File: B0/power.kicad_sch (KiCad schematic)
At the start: 54 parts, among them U001 74HCT00, U002 74HCT125, U007 74HCT32, U008 74HCT04, U009 74HCT00, U010 74HCT125, U011 74HCT04, U012 74HCT00, U013 74HCT125, U014 74HCT08, U015 74HCT04, U016 74HCT00, U017 74HCT125, U018 74HCT04, U019 74HCT00, U020 74HCT125, U021 74HCT08, U028 74HCT00, U029 74HCT00, U030 74HCT32, U031 74HCT00, U032 74HCT74

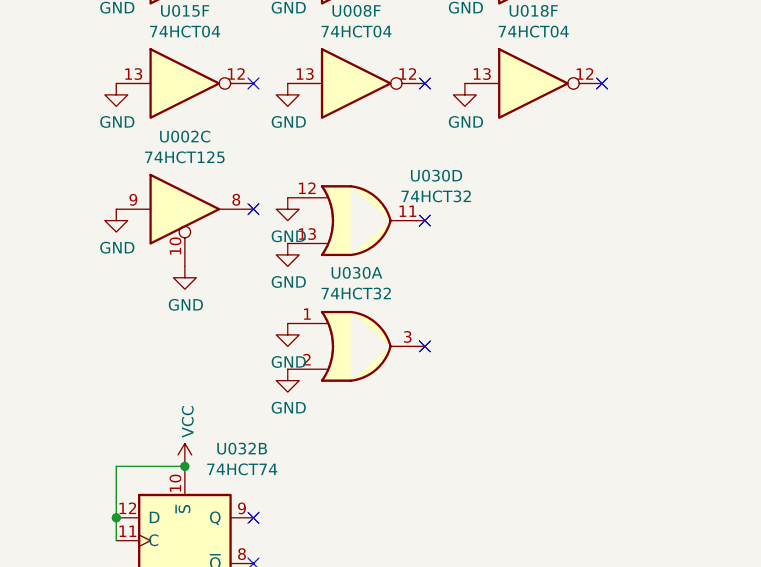
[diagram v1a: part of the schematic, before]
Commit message: B1 CREGA added
Work started on b1. CREGA added.
Minor changes to B0 schematic properties.
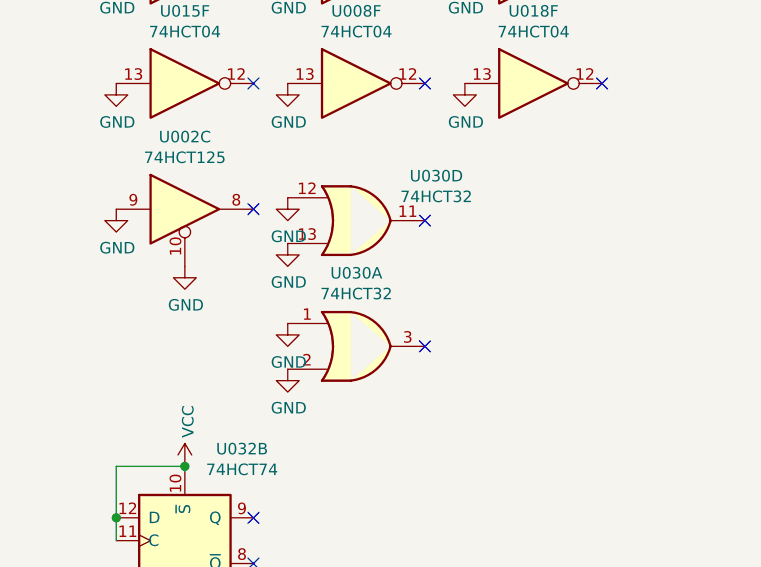
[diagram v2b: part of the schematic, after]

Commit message: .
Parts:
- C001, C002, C003, C004, C005, C006, C007, C008, C009, C010, C011, C012, C013, C014, C015, C016, C017, C018, C019, C020, C021, C022, C023, C024, C025, C026, C027, C028, C029, C030, C031, C032: value C -> 100n
- U007, U030: value 74HCT32 -> 74HC32
- U008, U011, U015, U018: value 74HCT04 -> 74HC04
- U009, U012, U016, U019, U028, U029, U031: value 74HCT00 -> 74HC00
- U010, U013, U017, U020: value 74HCT125 -> 74HC125
- U032: value 74HCT74 -> 74HC74
